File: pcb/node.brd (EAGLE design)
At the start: 50 x 68.5 mm, 19 parts, among them IC1 7805DT, J1 RJ11, J2 RJ11

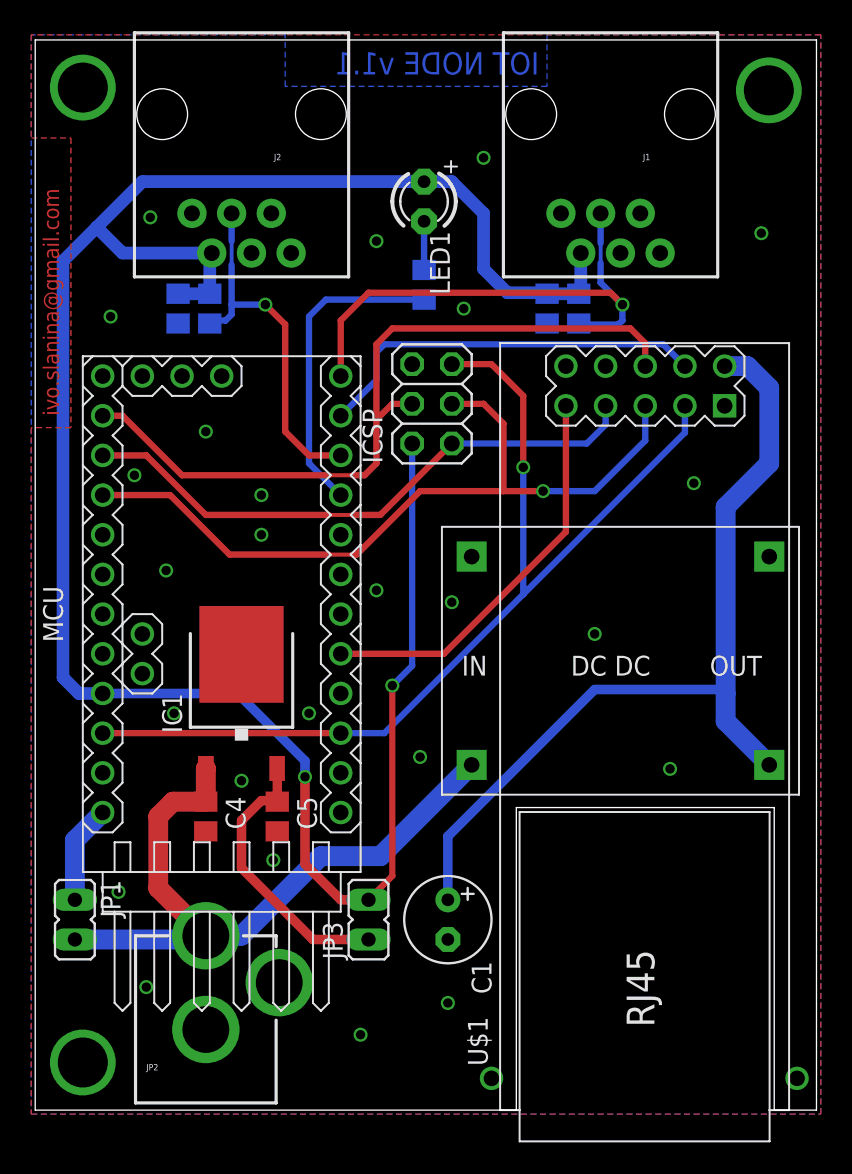
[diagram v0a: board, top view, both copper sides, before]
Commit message: Changed arduino footprint. Removed drills for unnecessary pins.
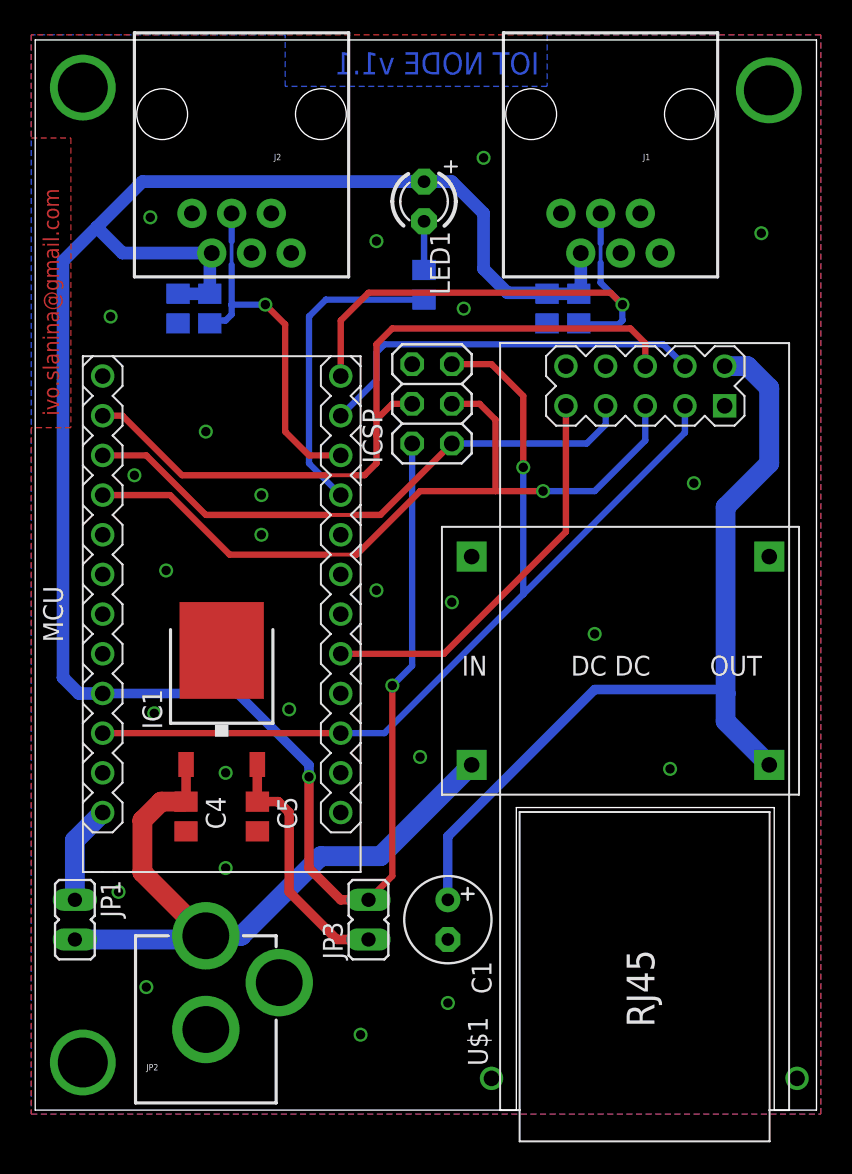
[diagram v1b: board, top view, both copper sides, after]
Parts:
- MCU: value ARDUINO-PRO-MINI-5.0V#APC -> ARDUINO-PRO-MINI-5.0V#SMP; device diy-modules:ARDUINO-PRO-MINI#APC -> diy-modules:ARDUINO-PRO-MINI#SMP
- R1: value (none) -> 150R
- moved IC1 1.30 mm to (11.9, 26.9)
- moved C4 1.27 mm to (9.65, 18.8)
- moved C5 1.27 mm to (14.2, 18.8)
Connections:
- net GND: no longer MCU.J3.1
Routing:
- net N$3: track 18.0 -> 16.1 mm
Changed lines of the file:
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@@
 <elements>
 <element name="ICSP" library="pinhead" package="2X03" value="" x="25.4" y="45.212" locked="yes" rot="R90"/>
-<element name="MCU" library="diy-modules" package="ARDUINO-PRO-MINI#APC" value="ARDUINO-PRO-MINI-5.0V#APC" x="11.938" y="31.75" rot="R90"/>
+<element name="MCU" library="diy-modules" package="ARDUINO-PRO-MINI#SMP" value="ARDUINO-PRO-MINI-5.0V#SMP" x="11.938" y="31.75" rot="R90"/>
 <element name="JP2" library="SparkFun-Connectors" package="POWER_JACK_PTH" value="POWER_JACKPTH" x="10.922" y="-2.54" locked="yes">
 <attribute name="PROD_ID" value="CONN-08197" x="70.612" y="-53.34" size="1.778" layer="27" display="off"/>
@@
 <element name="U$2" library="OK1CDJ-E6" package="DC-DC" value="DC-DC-SMALL" x="26.67" y="20.828"/>
 <element name="LED1" library="adafruit" package="LED3MM" value="" x="24.892" y="58.166" locked="yes" rot="R270"/>
-<element name="R1" library="rcl" package="R0805" value="" x="24.892" y="52.832" rot="MR270"/>
+<element name="R1" library="rcl" package="R0805" value="150R" x="24.892" y="52.832" rot="MR270"/>
 <element name="C2" library="rcl" package="C0805" value="100nF" x="9.144" y="51.308" rot="MR270"/>
 <element name="C3" library="rcl" package="C0805" value="100nF" x="32.766" y="51.308" rot="MR270"/>
@@
 <element name="R2" library="rcl" package="R0805" value="10k" x="34.798" y="51.308" rot="MR90"/>
 <element name="R3" library="rcl" package="R0805" value="10k" x="11.176" y="51.308" rot="MR90"/>
-<element name="IC1" library="linear" package="TO252" value="7805DT" x="13.208" y="26.67"/>
-<element name="C4" library="rcl" package="C0805" value="300nF" x="10.922" y="18.796" rot="R270"/>
-<element name="C5" library="rcl" package="C0805" value="100nF" x="15.494" y="18.796" rot="R270"/>
+<element name="IC1" library="linear" package="TO252" value="7805DT" x="11.938" y="26.924"/>
+<element name="C4" library="rcl" package="C0805" value="300nF" x="9.652" y="18.796" rot="R270"/>
+<element name="C5" library="rcl" package="C0805" value="100nF" x="14.224" y="18.796" rot="R270"/>
 <element name="JP1" library="jumper" package="JP1" value="" x="2.54" y="12.192" rot="R180"/>
 <element name="JP3" library="jumper" package="JP1" value="" x="21.336" y="12.192"/>
@@
 <signals>
 <signal name="GND">
-<contactref element="MCU" pad="J3.1"/>
 <contactref element="MCU" pad="J7.9"/>
 <contactref element="MCU" pad="J6.2"/>
@@
 <via x="35.814" y="30.48" extent="1-16" drill="0.6"/>
 <via x="40.64" y="21.844" extent="1-16" drill="0.6"/>
-<via x="8.89" y="25.4" extent="1-16" drill="0.6"/>
-<via x="13.208" y="21.082" extent="1-16" drill="0.6"/>
+<via x="7.62" y="25.4" extent="1-16" drill="0.6"/>
+<via x="12.192" y="21.59" extent="1-16" drill="0.6"/>
 <via x="7.112" y="7.874" extent="1-16" drill="0.6"/>
 <via x="20.828" y="4.826" extent="1-16" drill="0.6"/>
@@
 <via x="14.478" y="36.83" extent="1-16" drill="0.6"/>
 <via x="8.382" y="34.544" extent="1-16" drill="0.6"/>
-<via x="17.526" y="25.4" extent="1-16" drill="0.6"/>
+<via x="16.256" y="25.654" extent="1-16" drill="0.6"/>
 <via x="46.482" y="56.134" extent="1-16" drill="0.6"/>
 <via x="7.366" y="57.15" extent="1-16" drill="0.6"/>
 <via x="6.35" y="40.64" extent="1-16" drill="0.6"/>
 <via x="5.334" y="13.97" extent="1-16" drill="0.6"/>
-<via x="15.24" y="16.002" extent="1-16" drill="0.6"/>
+<via x="12.192" y="15.494" extent="1-16" drill="0.6"/>
 <via x="27.432" y="51.308" extent="1-16" drill="0.6"/>
 </signal>
@@
 <contactref element="C4" pad="1"/>
 <contactref element="JP1" pad="2"/>
-<wire x1="10.922" y1="19.746" x2="10.922" y2="21.864" width="1.27" layer="1"/>
-<wire x1="10.922" y1="21.864" x2="10.928" y2="21.87" width="1.27" layer="1"/>
 <wire x1="2.54" y1="10.922" x2="10.684" y2="10.922" width="1.27" layer="16"/>
 <wire x1="10.684" y1="10.922" x2="10.922" y2="11.16" width="1.27" layer="16"/>
@@
 <wire x1="18.288" y1="16.256" x2="22.098" y2="16.256" width="1.27" layer="16"/>
 <wire x1="22.098" y1="16.256" x2="27.94" y2="22.098" width="1.27" layer="16"/>
-<wire x1="10.922" y1="19.746" x2="8.824" y2="19.746" width="1.27" layer="1"/>
-<wire x1="8.824" y1="19.746" x2="7.874" y2="18.796" width="1.27" layer="1"/>
-<wire x1="7.874" y1="18.796" x2="7.874" y2="14.208" width="1.27" layer="1"/>
-<wire x1="7.874" y1="14.208" x2="10.922" y2="11.16" width="1.27" layer="1"/>
+<wire x1="9.652" y1="19.746" x2="8.062" y2="19.746" width="1.27" layer="1"/>
+<wire x1="8.062" y1="19.746" x2="6.858" y2="18.542" width="1.27" layer="1"/>
+<wire x1="6.858" y1="18.542" x2="6.858" y2="15.224" width="1.27" layer="1"/>
+<wire x1="6.858" y1="15.224" x2="10.922" y2="11.16" width="1.27" layer="1"/>
+<wire x1="9.658" y1="22.124" x2="9.658" y2="19.752" width="0.6096" layer="1"/>
+<wire x1="9.658" y1="19.752" x2="9.652" y2="19.746" width="0.6096" layer="1"/>
 </signal>
 <signal name="MISO">
@@
 <wire x1="20.32" y1="35.56" x2="20.574" y2="35.56" width="0.4064" layer="1"/>
 <wire x1="20.574" y1="35.56" x2="24.638" y2="39.624" width="0.4064" layer="1"/>
-<wire x1="24.638" y1="39.624" x2="29.972" y2="39.624" width="0.4064" layer="1"/>
+<wire x1="24.638" y1="39.624" x2="29.464" y2="39.624" width="0.4064" layer="1"/>
 <via x="32.512" y="39.624" extent="1-16" drill="0.6"/>
-<wire x1="29.972" y1="39.624" x2="32.512" y2="39.624" width="0.4064" layer="1"/>
+<wire x1="29.464" y1="39.624" x2="32.512" y2="39.624" width="0.4064" layer="1"/>
 <wire x1="32.512" y1="39.624" x2="35.814" y2="39.624" width="0.4064" layer="16"/>
 <wire x1="35.814" y1="39.624" x2="39.0525" y2="42.8625" width="0.4064" layer="16"/>
-<wire x1="26.67" y1="45.212" x2="28.702" y2="45.212" width="0.4064" layer="1"/>
-<wire x1="28.702" y1="45.212" x2="29.972" y2="43.942" width="0.4064" layer="1"/>
-<wire x1="29.972" y1="43.942" x2="29.972" y2="39.624" width="0.4064" layer="1"/>
 <wire x1="39.0525" y1="45.085" x2="39.0525" y2="42.8625" width="0.4064" layer="16"/>
+<wire x1="26.67" y1="45.212" x2="28.448" y2="45.212" width="0.4064" layer="1"/>
+<wire x1="28.448" y1="45.212" x2="29.464" y2="44.196" width="0.4064" layer="1"/>
+<wire x1="29.464" y1="44.196" x2="29.464" y2="39.624" width="0.4064" layer="1"/>
 </signal>
 <signal name="RESET">
@@
 <wire x1="28.702" y1="53.848" x2="30.226" y2="52.324" width="0.8128" layer="16"/>
 <wire x1="21.336" y1="13.462" x2="19.558" y2="13.462" width="0.6096" layer="1"/>
-<wire x1="19.558" y1="13.462" x2="17.272" y2="15.748" width="0.6096" layer="1"/>
-<wire x1="17.272" y1="15.748" x2="17.272" y2="21.336" width="0.6096" layer="1"/>
-<via x="17.272" y="21.336" extent="1-16" drill="0.6"/>
-<wire x1="17.272" y1="21.336" x2="17.272" y2="22.352" width="0.6096" layer="16"/>
-<wire x1="17.272" y1="22.352" x2="12.954" y2="26.67" width="0.6096" layer="16"/>
+<wire x1="17.526" y1="22.098" x2="12.954" y2="26.67" width="0.6096" layer="16"/>
 <wire x1="12.954" y1="26.67" x2="4.318" y2="26.67" width="0.6096" layer="16"/>
 <wire x1="30.226" y1="52.324" x2="32.7" y2="52.324" width="0.8128" layer="16"/>
@@
 <wire x1="22.86" y1="27.178" x2="22.86" y2="14.986" width="0.4064" layer="1"/>
 <wire x1="22.86" y1="14.986" x2="21.336" y2="13.462" width="0.4064" layer="1"/>
+<wire x1="19.558" y1="13.462" x2="17.526" y2="15.494" width="0.6096" layer="1"/>
+<wire x1="17.526" y1="15.494" x2="17.526" y2="21.336" width="0.6096" layer="1"/>
+<via x="17.526" y="21.336" extent="1-16" drill="0.6"/>
+<wire x1="17.526" y1="21.336" x2="17.526" y2="22.098" width="0.6096" layer="16"/>
 </signal>
 <signal name="ENC28J60_DATA_INT">
@@
 <contactref element="C5" pad="1"/>
 <contactref element="JP3" pad="1"/>
-<wire x1="15.494" y1="19.746" x2="15.494" y2="21.864" width="0.6096" layer="1"/>
-<wire x1="15.494" y1="21.864" x2="15.488" y2="21.87" width="0.6096" layer="1"/>
-<wire x1="21.336" y1="10.922" x2="17.78" y2="10.922" width="0.6096" layer="1"/>
-<wire x1="17.78" y1="10.922" x2="13.208" y2="15.494" width="0.6096" layer="1"/>
-<wire x1="13.208" y1="15.494" x2="13.208" y2="18.542" width="0.6096" layer="1"/>
-<wire x1="13.208" y1="18.542" x2="14.478" y2="19.812" width="0.6096" layer="1"/>
-<wire x1="14.478" y1="19.812" x2="15.428" y2="19.812" width="0.6096" layer="1"/>
-<wire x1="15.428" y1="19.812" x2="15.494" y2="19.746" width="0.6096" layer="1"/>
+<wire x1="14.218" y1="22.124" x2="14.218" y2="19.752" width="0.6096" layer="1"/>
+<wire x1="14.218" y1="19.752" x2="14.224" y2="19.746" width="0.6096" layer="1"/>
+<wire x1="14.224" y1="19.746" x2="15.56" y2="19.746" width="0.6096" layer="1"/>
+<wire x1="15.56" y1="19.746" x2="16.256" y2="19.05" width="0.6096" layer="1"/>
+<wire x1="16.256" y1="19.05" x2="16.256" y2="13.97" width="0.6096" layer="1"/>
+<wire x1="16.256" y1="13.97" x2="19.304" y2="10.922" width="0.6096" layer="1"/>
+<wire x1="19.304" y1="10.922" x2="21.336" y2="10.922" width="0.6096" layer="1"/>
 </signal>
 </signals>

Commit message: Final release.
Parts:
- renumbered JP1 to IVR, JP3 to EVR

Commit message: Some formal changes.
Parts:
- C1: value (none) -> 220uF
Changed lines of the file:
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@@
 <attribute name="VALUE" x="35.306" y="52.578" size="1.27" layer="28" rot="MR270"/>
 </element>
-<element name="C1" library="rcl" package="E2,5-6" value="" x="26.416" y="12.192" smashed="yes" rot="R270">
+<element name="C1" library="rcl" package="E2,5-6" value="220uF" x="26.416" y="12.192" smashed="yes" rot="R270">
 <attribute name="NAME" x="25.527" y="7.874" size="1.27" layer="25" font="vector" ratio="15"/>
 <attribute name="VALUE" x="23.749" y="9.525" size="1.27" layer="27" ratio="10" rot="R270"/>

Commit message: Changed voltage regulator input capacitor value.
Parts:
- C4: value 300nF -> 330nF
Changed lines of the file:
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@@
 <attribute name="VALUE" x="17.018" y="24.384" size="1.27" layer="27" rot="R90"/>
 </element>
-<element name="C4" library="rcl" package="C0805" value="300nF" x="9.652" y="18.796" smashed="yes" rot="R270">
+<element name="C4" library="rcl" package="C0805" value="330nF" x="9.652" y="18.796" smashed="yes" rot="R270">
 <attribute name="NAME" x="10.922" y="16.51" size="1.27" layer="25" font="vector" ratio="15" rot="R180"/>
 <attribute name="VALUE" x="7.112" y="20.066" size="1.27" layer="27" rot="R270"/>

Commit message: Changed notification LED current limiting resistor value.
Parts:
- R1: value 150R -> 180R
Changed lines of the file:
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@@
 <attribute name="VALUE" x="23.241" y="56.261" size="1.27" layer="27" ratio="10" rot="R270"/>
 </element>
-<element name="R1" library="rcl" package="R0805" value="150R" x="24.892" y="52.832" smashed="yes" rot="MR270">
+<element name="R1" library="rcl" package="R0805" value="180R" x="24.892" y="52.832" smashed="yes" rot="MR270">
 <attribute name="NAME" x="23.495" y="50.8" size="1.27" layer="26" font="vector" ratio="15" rot="MR180"/>
 <attribute name="VALUE" x="27.432" y="53.467" size="1.27" layer="28" rot="MR270"/>

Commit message: Fixed some part names. Changed board label.
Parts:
- renumbered U$1 to ETHERNET
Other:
- board text added: "AVR ENC28J60 NODE v1.1.1"
- board text removed: "IOT NODE v1.1"
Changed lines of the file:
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@@
 <wire x1="50.0126" y1="68.5038" x2="0" y2="68.5038" width="0" layer="20"/>
 <wire x1="0" y1="68.5038" x2="0" y2="0" width="0" layer="20"/>
-<text x="32.258" y="66.294" size="1.4224" layer="22" font="vector" ratio="15" rot="MR0">IOT NODE v1.1</text>
+<text x="24.892" y="66.802" size="1.4224" layer="22" font="vector" ratio="15" rot="MR0" align="center">AVR ENC28J60 NODE v1.1.1</text>
 <text x="1.524" y="44.45" size="1.016" layer="21" font="vector" ratio="15" rot="R90">ivo.slanina@gmail.com</text>
 </plain>
@@
 <attribute name="VALUE" x="7.112" y="1.27" size="0.4064" layer="27"/>
 </element>
-<element name="U$1" library="diy-modules" package="ETHERNET-ENC28J60-MINI" value="ETHERNET-ENC28J60-MINI" x="48.26" y="0" locked="yes" smashed="yes" rot="R90">
-<attribute name="NAME" x="28.97" y="4.4" size="1.27" layer="25" font="vector" ratio="15" rot="R90" align="bottom-center"/>
+<element name="ETHERNET" library="diy-modules" package="ETHERNET-ENC28J60-MINI" value="ETHERNET-ENC28J60-MINI" x="48.26" y="0" locked="yes" smashed="yes" rot="R90">
+<attribute name="NAME" x="35.224" y="21.858" size="1.27" layer="25" font="vector" ratio="15" rot="R180" align="bottom-center"/>
 <attribute name="VALUE" x="49.53" y="25.4" size="1.27" layer="27" rot="R90" align="top-center"/>
 </element>
@@
 <contactref element="J1" pad="2"/>
 <contactref element="J2" pad="2"/>
-<contactref element="U$1" pad="GND"/>
+<contactref element="ETHERNET" pad="GND"/>
 <contactref element="JP2" pad="GND"/>
 <contactref element="JP2" pad="GNDBREAK"/>
@@
 <contactref element="MCU" pad="J6.10"/>
 <contactref element="ICSP" pad="1"/>
-<contactref element="U$1" pad="SO"/>
+<contactref element="ETHERNET" pad="SO"/>
 <wire x1="36.5125" y1="45.085" x2="36.5125" y2="43.8785" width="0.4064" layer="16"/>
 <wire x1="36.5125" y1="43.8785" x2="35.306" y2="42.672" width="0.4064" layer="16"/>
@@
 <contactref element="MCU" pad="J6.11"/>
 <contactref element="ICSP" pad="4"/>
-<contactref element="U$1" pad="SI"/>
+<contactref element="ETHERNET" pad="SI"/>
 <wire x1="4.318" y1="44.45" x2="5.588" y2="44.45" width="0.4064" layer="1"/>
 <wire x1="5.588" y1="44.45" x2="9.398" y2="40.64" width="0.4064" layer="1"/>
@@
 <contactref element="MCU" pad="J6.9"/>
 <contactref element="ICSP" pad="3"/>
-<contactref element="U$1" pad="SCK"/>
+<contactref element="ETHERNET" pad="SCK"/>
 <wire x1="4.318" y1="39.37" x2="8.636" y2="39.37" width="0.4064" layer="1"/>
 <wire x1="8.636" y1="39.37" x2="12.446" y2="35.56" width="0.4064" layer="1"/>
@@
 <contactref element="MCU" pad="J7.10"/>
 <contactref element="ICSP" pad="5"/>
-<contactref element="U$1" pad="RST"/>
+<contactref element="ETHERNET" pad="RST"/>
 <contactref element="MCU" pad="J6.3"/>
 <wire x1="4.318" y1="24.13" x2="19.558" y2="24.13" width="0.4064" layer="1"/>
@@
 <signal name="ENC28J60_CS">
 <contactref element="MCU" pad="J7.2"/>
-<contactref element="U$1" pad="CS"/>
+<contactref element="ETHERNET" pad="CS"/>
 <wire x1="19.558" y1="44.45" x2="21.844" y2="46.736" width="0.4064" layer="16"/>
 <wire x1="21.844" y1="46.736" x2="21.844" y2="48.514" width="0.4064" layer="16"/>
@@
 </signal>
 <signal name="+3V3">
-<contactref element="U$1" pad="VCC"/>
+<contactref element="ETHERNET" pad="VCC"/>
 <contactref element="U$2" pad="P$2"/>
 <contactref element="C1" pad="+"/>
@@
 <signal name="ENC28J60_DATA_INT">
 <contactref element="MCU" pad="J7.8"/>
-<contactref element="U$1" pad="INT"/>
+<contactref element="ETHERNET" pad="INT"/>
 <wire x1="33.9725" y1="45.085" x2="33.9725" y2="37.0205" width="0.4064" layer="1"/>
 <wire x1="33.9725" y1="37.0205" x2="26.162" y2="29.21" width="0.4064" layer="1"/>
